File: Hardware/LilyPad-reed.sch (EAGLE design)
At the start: 7 parts

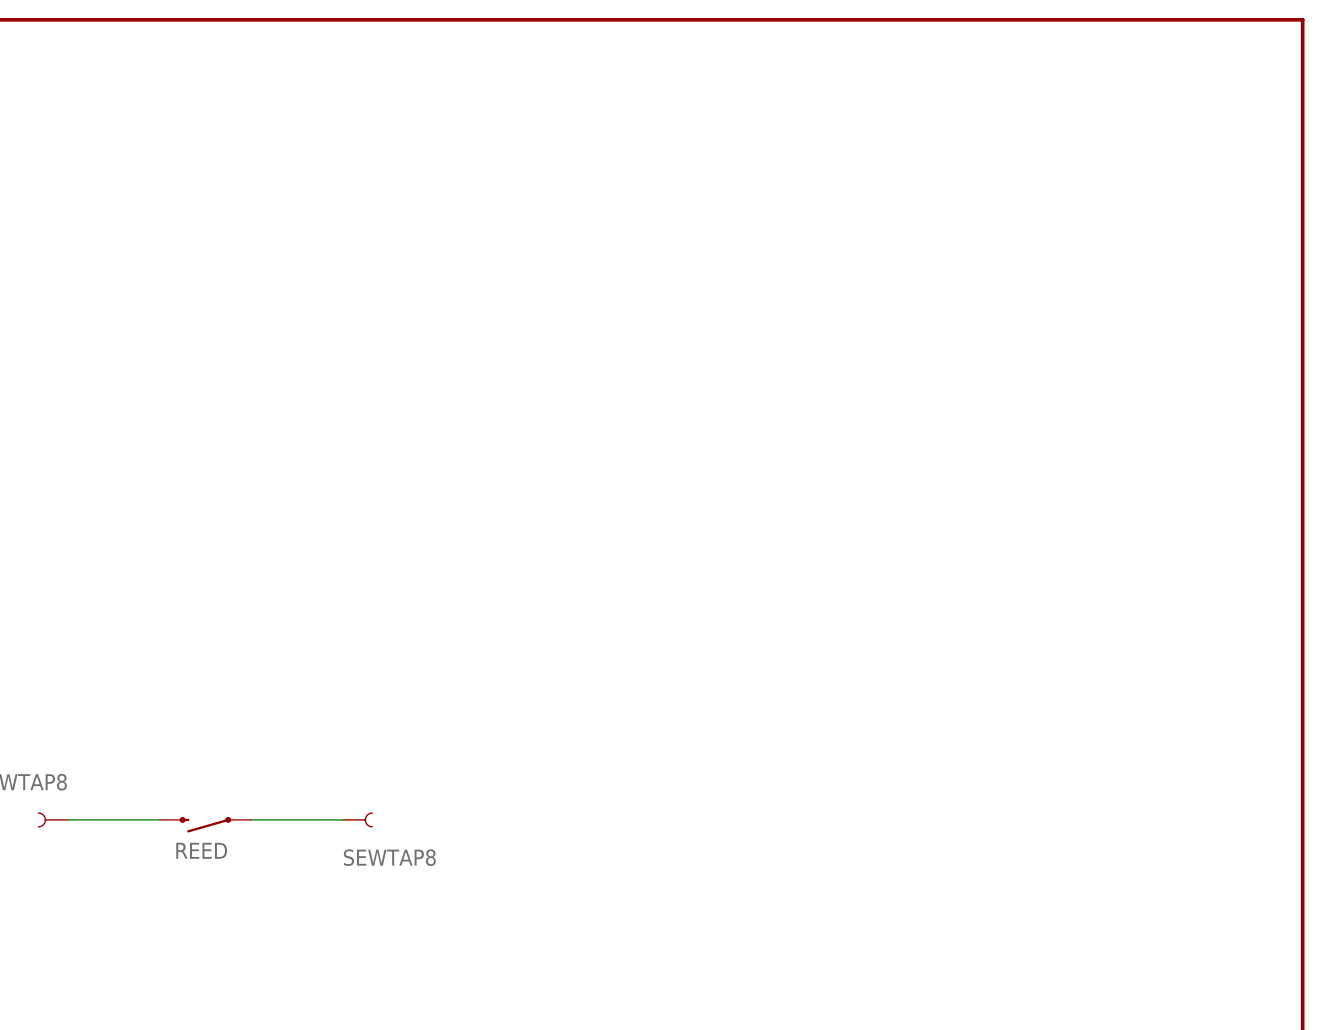
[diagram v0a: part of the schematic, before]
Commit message: QC checklist changes
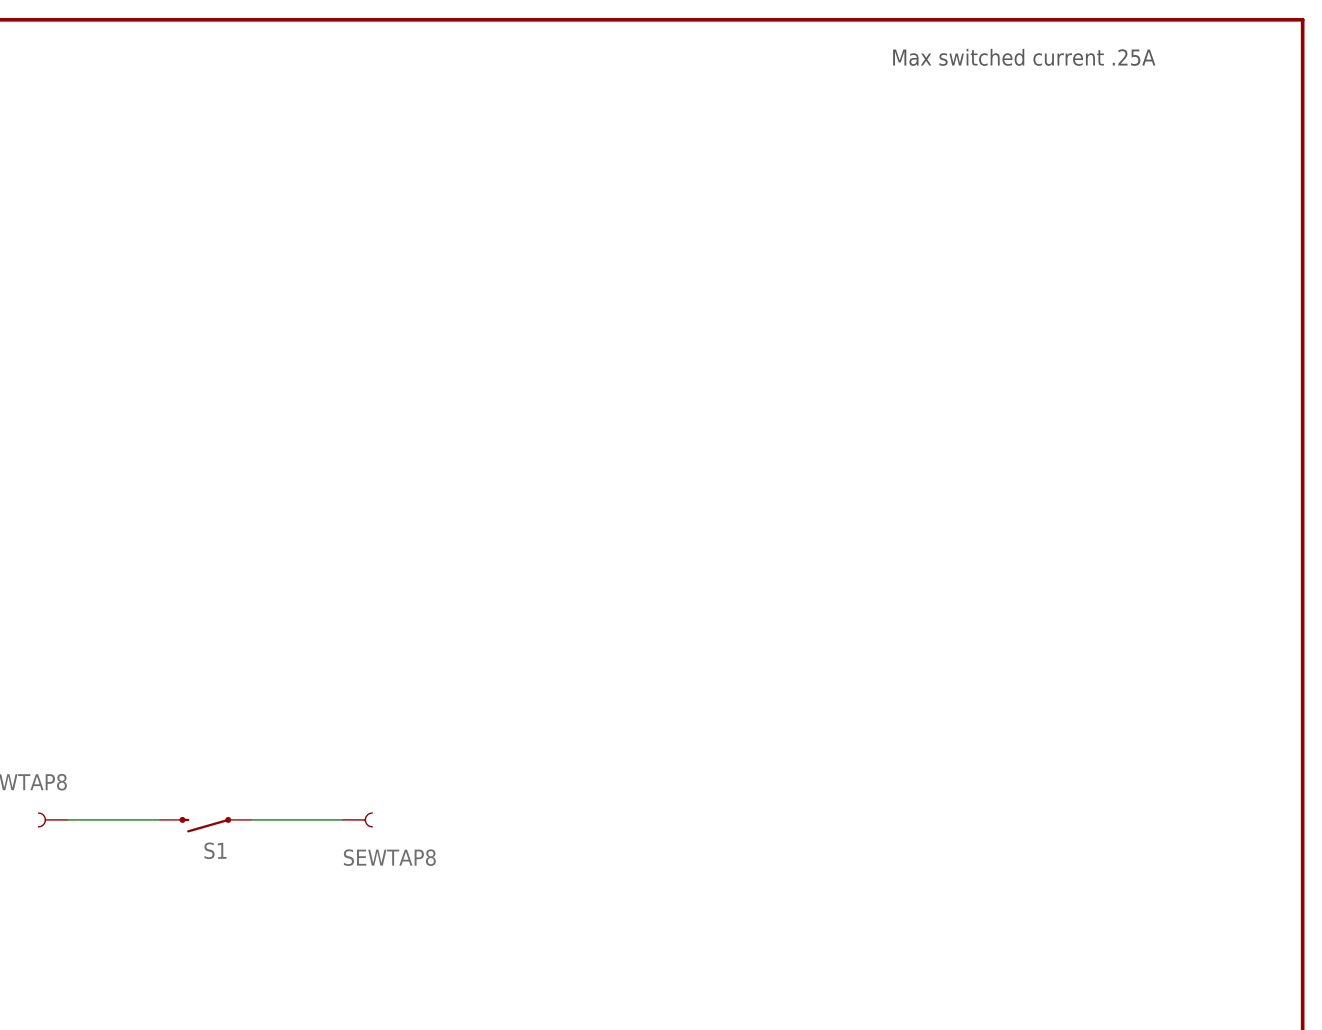
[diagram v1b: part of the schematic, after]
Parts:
- S1: value SWITCH-MOMENTARY-2PTH_REED2 -> REED
- renumbered REED to S1
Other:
- note added: "Max switched current .25A"
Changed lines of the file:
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@@
 <part name="SLIDEOFF" library="LilyPad-Wearables" deviceset="SEWTAP" device="8"/>
 <part name="SLIDEON" library="LilyPad-Wearables" deviceset="SEWTAP" device="8"/>
-<part name="REED" library="SparkFun-Electromechanical" deviceset="SWITCH-MOMENTARY-2" device="PTH_REED2"/>
+<part name="S1" library="SparkFun-Electromechanical" deviceset="SWITCH-MOMENTARY-2" device="PTH_REED2" value="REED"/>
 <part name="U$1" library="LilyPad-Wearables" deviceset="LOGO-LP" device="LP"/>
 <part name="LOGO1" library="SparkFun-Aesthetics" deviceset="OSHW-LOGO" device="S-COPPER"/>
@@
 <text x="177.8" y="7.62" size="3.81" layer="94">Dia Campbell</text>
 <text x="239.522" y="6.858" size="3.81" layer="94">01</text>
+<text x="203.2" y="180.34" size="1.778" layer="97">Max switched current .25A</text>
 </plain>
 <instances>
@@
 <attribute name="VALUE" x="142.24" y="91.44" size="1.778" layer="96"/>
 </instance>
-<instance part="REED" gate="G$1" x="127" y="96.52" smashed="yes" rot="R180">
+<instance part="S1" gate="G$1" x="127" y="96.52" smashed="yes" rot="R180">
 <attribute name="NAME" x="129.54" y="93.98" size="1.778" layer="95" rot="R180"/>
 </instance>
@@
 <segment>
 <pinref part="SLIDEOFF" gate="G$1" pin="1"/>
-<pinref part="REED" gate="G$1" pin="2"/>
+<pinref part="S1" gate="G$1" pin="2"/>
 <wire x1="111.76" y1="96.52" x2="121.92" y2="96.52" width="0.1524" layer="91"/>
 </segment>
@@
 <net name="N$2" class="0">
 <segment>
-<pinref part="REED" gate="G$1" pin="1"/>
+<pinref part="S1" gate="G$1" pin="1"/>
 <pinref part="SLIDEON" gate="G$1" pin="1"/>
 <wire x1="132.08" y1="96.52" x2="142.24" y2="96.52" width="0.1524" layer="91"/>

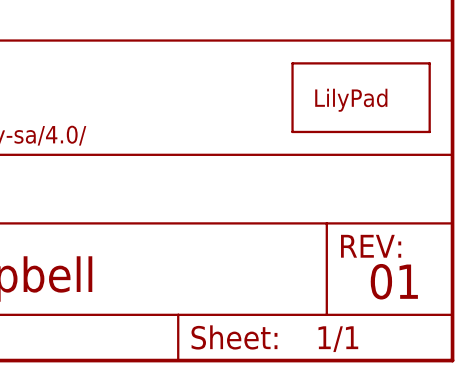
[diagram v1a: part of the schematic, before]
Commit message: Fixed version number for redboards
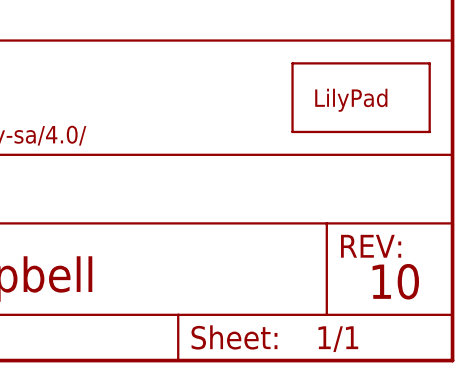
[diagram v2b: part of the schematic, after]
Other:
- note added: "10"
- note removed: "01"
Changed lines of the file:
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@@
 <plain>
 <text x="177.8" y="7.62" size="3.81" layer="94">Dia Campbell</text>
-<text x="239.522" y="6.858" size="3.81" layer="94">01</text>
+<text x="239.522" y="6.858" size="3.81" layer="94">10</text>
 <text x="203.2" y="180.34" size="1.778" layer="97">Max switched current .25A</text>
 </plain>
